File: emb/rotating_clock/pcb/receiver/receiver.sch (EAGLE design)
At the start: 23 parts, among them IC1 A1321LH, IC2 A1321LH, IC3 A1321LH, IC4 LM358D, IC5 LM358D

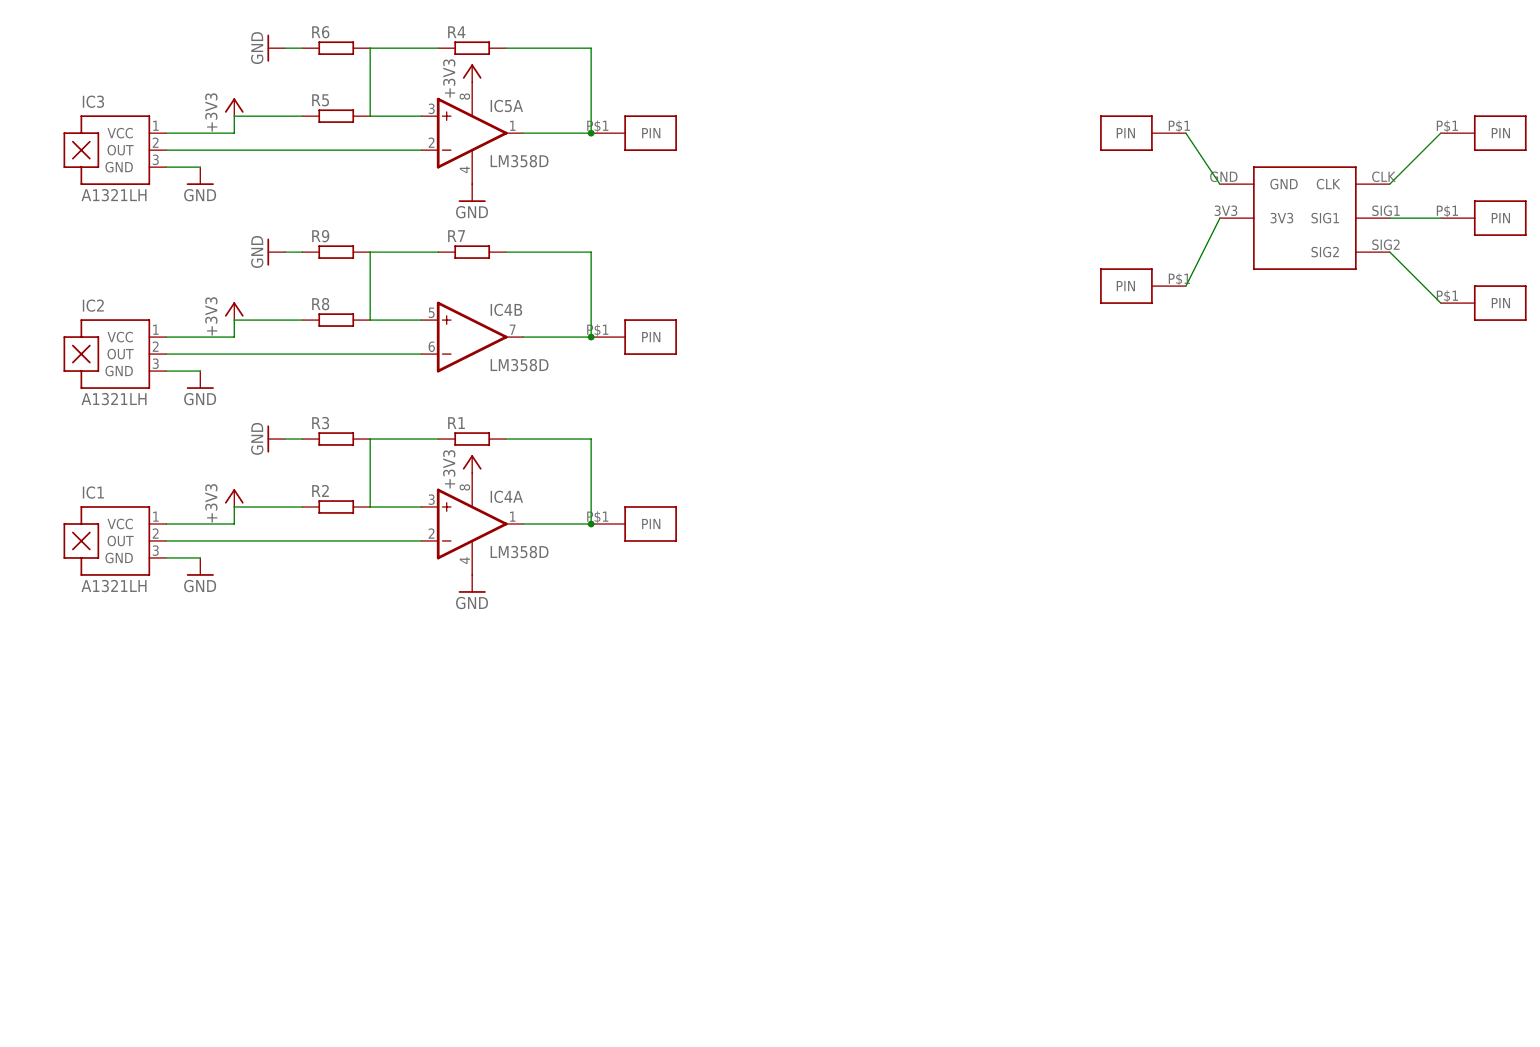
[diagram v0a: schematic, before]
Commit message: Updated bot board schematic
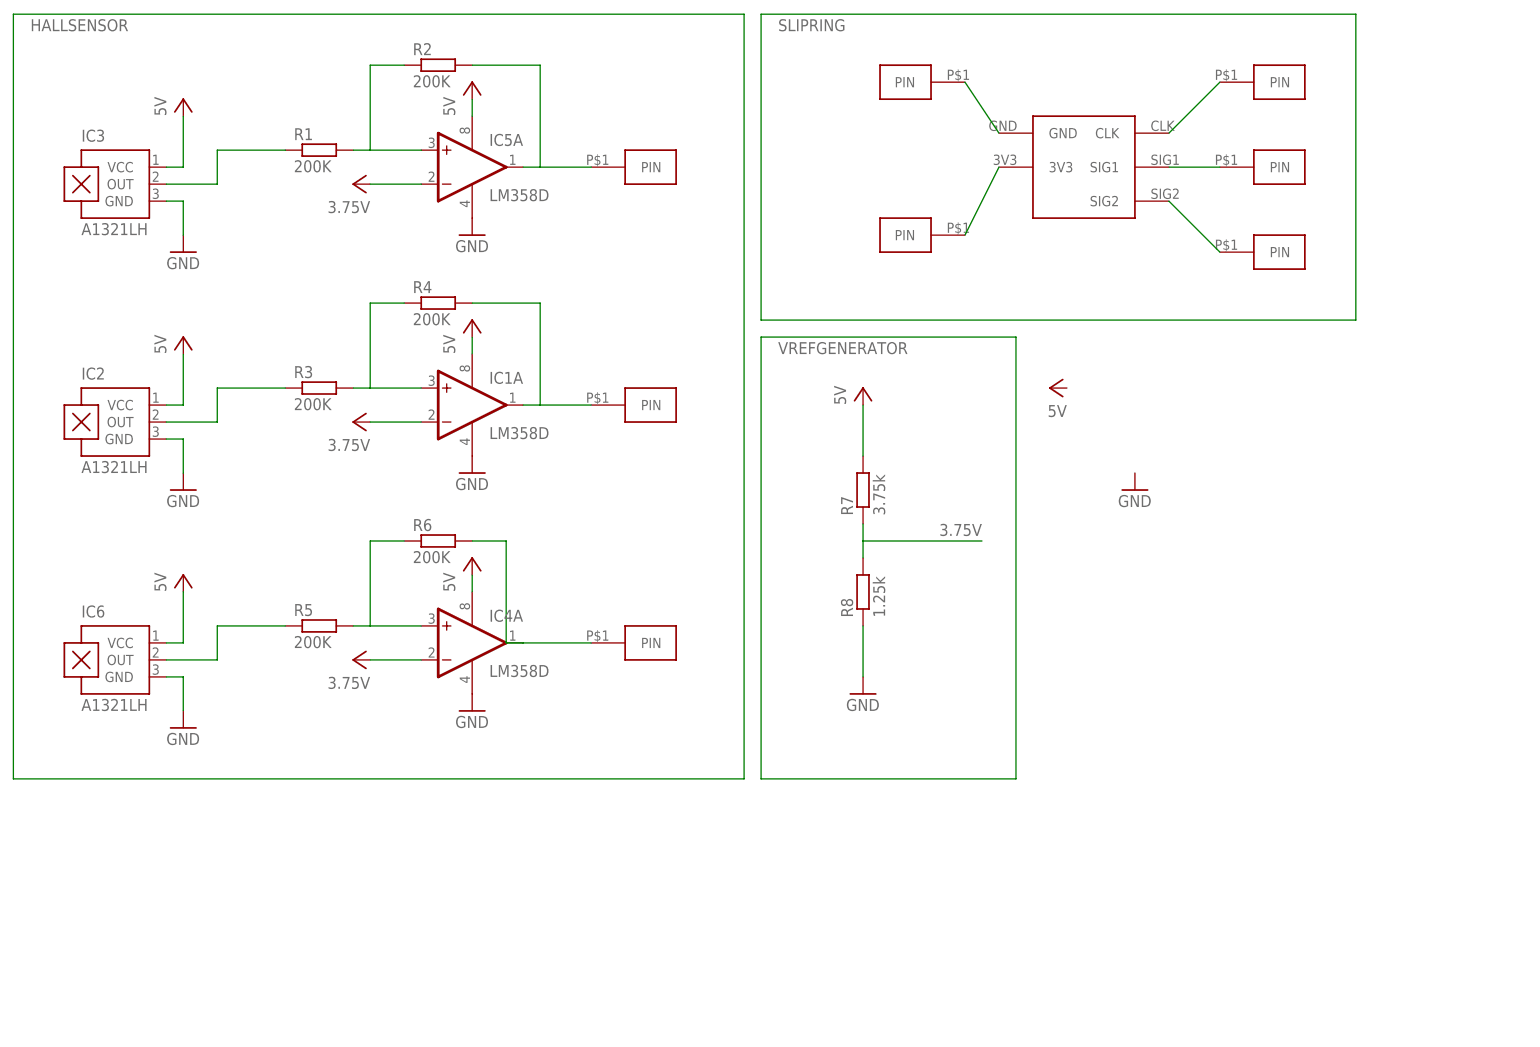
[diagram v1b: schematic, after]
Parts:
- removed R9: (no value), resistor:R-EU_R0805
- added IC6: A1321LH, allegro:A1321LH
- IC1: value A1321LH -> LM358D; device allegro:A1321LH -> linear:LM358D
- R1, R2, R3, R4, R5, R6: value (none) -> 200K
- R7: value (none) -> 3.75k
- R8: value (none) -> 1.25k
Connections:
- removed net +3V3: IC1.VCC, IC2.VCC, IC3.VCC, IC4P.V+, IC5P.V+, R2.1, R5.1, R8.1
- removed net N$2: IC4A.OUT, R1.2, U$4.PIN
- new net 3.75V: IC5A.-IN, R7.1, R8.2
- new net 5V: IC1P.V+, IC2.VCC, IC3.VCC, IC4P.V+, IC5P.V+, IC6.VCC, R7.2
- new net R20: IC1A.+IN, R3.2, R4.1
- new net VCC: IC1A.-IN, IC4A.-IN
- net GND: now also IC1P.V-, IC6.GND, R8.1; no longer IC1.GND, R3.1, R6.1, R9.1
- net N$1: now also IC2.OUT, R3.1; no longer IC4A.+IN, R1.1, R2.2, R3.2
- net N$3: now also IC1A.OUT, R4.2, U$3.PIN; no longer IC1.OUT, IC4A.-IN
- net N$4: now also IC3.OUT, R1.1; no longer IC5A.+IN, R4.1, R5.2, R6.2
- net N$5: now also IC5A.+IN, R1.2, R2.1; no longer IC5A.OUT, R4.2, U$2.PIN
- net N$6: now also IC5A.OUT, R2.2, U$2.PIN; no longer IC3.OUT, IC5A.-IN
- net N$7: now also IC6.OUT, R5.1; no longer IC4B.+IN, R7.1, R8.2, R9.2
- net N$8: now also IC4A.+IN, R5.2, R6.1; no longer IC4B.OUT, R7.2, U$3.PIN
- net N$9: now also IC4A.OUT, R6.2, U$4.PIN; no longer IC2.OUT, IC4B.-IN
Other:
- moved on the sheet: IC2, IC3, IC4A, IC5A, R1, R2, R3, R4, R5, R6, R7, R8

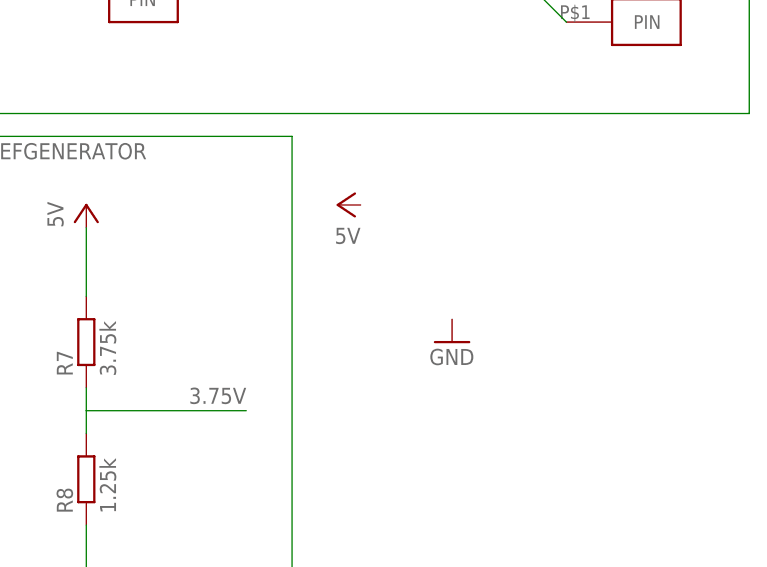
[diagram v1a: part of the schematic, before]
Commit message: Updated bot board schematic
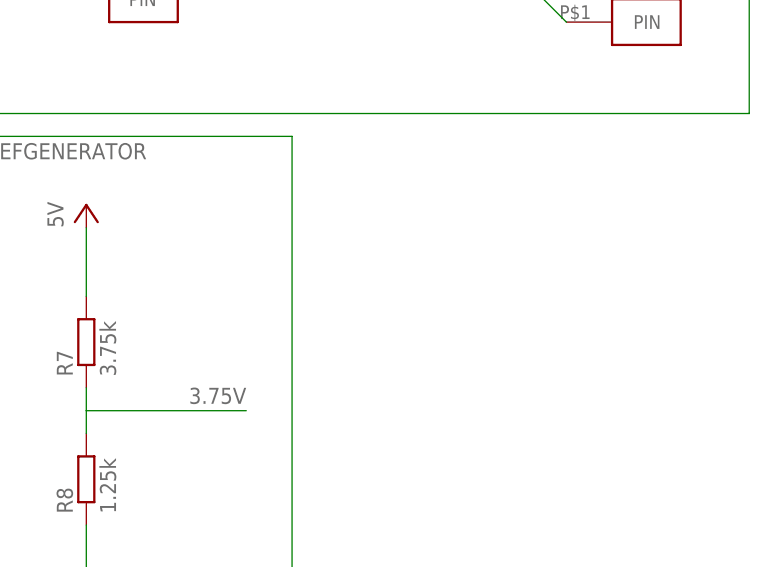
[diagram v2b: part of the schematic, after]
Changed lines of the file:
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@@
 <part name="R8" library="resistor" deviceset="R-EU_" device="R0805" value="1.25k"/>
 <part name="GND6" library="supply1" deviceset="GND" device=""/>
-<part name="P+5" library="supply1" deviceset="VCC" device="" value="5V"/>
-<part name="GND7" library="supply1" deviceset="GND" device=""/>
 </parts>
 <sheets>
@@
 <instance part="R8" gate="G$1" x="137.16" y="10.16" rot="R90"/>
 <instance part="GND6" gate="1" x="137.16" y="-5.08"/>
-<instance part="P+5" gate="VCC" x="165.1" y="40.64" rot="R90"/>
-<instance part="GND7" gate="1" x="177.8" y="25.4"/>
 </instances>
 <busses>

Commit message: Report stuff
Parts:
- R2, R4, R6: value 200K -> 1M
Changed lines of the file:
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@@
 <part name="U$9" library="slip_ring" deviceset="CONNECTOR" device=""/>
 <part name="R1" library="resistor" deviceset="R-EU_" device="R0805" value="200K"/>
-<part name="R2" library="resistor" deviceset="R-EU_" device="R0805" value="200K"/>
+<part name="R2" library="resistor" deviceset="R-EU_" device="R0805" value="1M"/>
 <part name="3.75" library="supply1" deviceset="VCC" device="" value="3.75V"/>
 <part name="P+1" library="supply1" deviceset="VCC" device="" value="5V"/>
@@
 <part name="U$3" library="slip_ring" deviceset="CONNECTOR" device=""/>
 <part name="R3" library="resistor" deviceset="R-EU_" device="R0805" value="200K"/>
-<part name="R4" library="resistor" deviceset="R-EU_" device="R0805" value="200K"/>
+<part name="R4" library="resistor" deviceset="R-EU_" device="R0805" value="1M"/>
 <part name="3.1" library="supply1" deviceset="VCC" device="" value="3.75V"/>
 <part name="P+2" library="supply1" deviceset="VCC" device="" value="5V"/>
@@
 <part name="U$4" library="slip_ring" deviceset="CONNECTOR" device=""/>
 <part name="R5" library="resistor" deviceset="R-EU_" device="R0805" value="200K"/>
-<part name="R6" library="resistor" deviceset="R-EU_" device="R0805" value="200K"/>
+<part name="R6" library="resistor" deviceset="R-EU_" device="R0805" value="1M"/>
 <part name="3.2" library="supply1" deviceset="VCC" device="" value="3.75V"/>
 <part name="P+3" library="supply1" deviceset="VCC" device="" value="5V"/>

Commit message: Report stuff
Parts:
- added PWM: PWM, slip_ring:CONNECTOR
- added Q1: NTD5867NL, adafruit:MOSFET-NGDS_TO220V
- added Q2, Q3, Q4: BSS138, SparkFun:MOSFET-NCHANNELSMD
- added R10, R11, R12, R13, R14, R9: 10K, SparkFun:RESISTOR0603-RES
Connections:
- removed net N$3: IC1A.OUT, R4.2, U$3.PIN
- removed net N$6: IC5A.OUT, R2.2, U$2.PIN
- removed net N$9: IC4A.OUT, R6.2, U$4.PIN
- new net 1: IC5A.OUT, R2.2
- new net 2: IC1A.OUT, R4.2
- new net 3: IC4A.OUT, R6.2
- new net HV: R10.1, R12.1, R14.1
- new net HV1: Q2.D, R10.2, U$4.PIN
- new net HV2: Q3.D, R12.2, U$2.PIN
- new net HV3: Q4.D, R14.2, U$3.PIN
- new net N$2: PWM.PIN
- new net OUT1: Q2.S, R9.2
- new net OUT2: Q3.S, R11.2
- new net OUT3: Q4.S, R13.2
- net GND: now also Q1.S
- net VCC: now also Q1.D, Q2.G, Q3.G, Q4.G, R11.1, R13.1, R9.1
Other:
- note added: "Motor"
- note added: "PWM"

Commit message: Reportstuff
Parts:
- Q2, Q3, Q4: value BSS138 -> NDT5867NLT4G
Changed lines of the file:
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@@
 <part name="GND7" library="supply1" deviceset="GND" device=""/>
 <part name="PWM" library="slip_ring" deviceset="CONNECTOR" device="" value="PWM"/>
-<part name="Q2" library="SparkFun" deviceset="MOSFET-NCHANNEL" device="SMD" value="BSS138"/>
+<part name="Q2" library="SparkFun" deviceset="MOSFET-NCHANNEL" device="SMD" value="NDT5867NLT4G"/>
 <part name="R9" library="SparkFun" deviceset="RESISTOR" device="0603-RES" value="10K"/>
 <part name="R10" library="SparkFun" deviceset="RESISTOR" device="0603-RES" value="10K"/>
@@
 <part name="P+7" library="SparkFun" deviceset="VCC" device="" value="5V"/>
 <part name="U$2" library="slip_ring" deviceset="CONNECTOR" device=""/>
-<part name="Q3" library="SparkFun" deviceset="MOSFET-NCHANNEL" device="SMD" value="BSS138"/>
+<part name="Q3" library="SparkFun" deviceset="MOSFET-NCHANNEL" device="SMD" value="NDT5867NLT4G"/>
 <part name="R11" library="SparkFun" deviceset="RESISTOR" device="0603-RES" value="10K"/>
 <part name="R12" library="SparkFun" deviceset="RESISTOR" device="0603-RES" value="10K"/>
@@
 <part name="P+9" library="SparkFun" deviceset="VCC" device="" value="5V"/>
 <part name="U$3" library="slip_ring" deviceset="CONNECTOR" device=""/>
-<part name="Q4" library="SparkFun" deviceset="MOSFET-NCHANNEL" device="SMD" value="BSS138"/>
+<part name="Q4" library="SparkFun" deviceset="MOSFET-NCHANNEL" device="SMD" value="NDT5867NLT4G"/>
 <part name="R13" library="SparkFun" deviceset="RESISTOR" device="0603-RES" value="10K"/>
 <part name="R14" library="SparkFun" deviceset="RESISTOR" device="0603-RES" value="10K"/>
